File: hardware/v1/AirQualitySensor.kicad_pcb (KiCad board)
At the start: 2 copper layers, 81.3 x 36.8 mm, 44 parts, among them J1 USB_C_Receptacle_USB2.0, J2 SWD, J3 UART, U1 004-0-0053, U2 DHT22, U3 XC6206P332MR

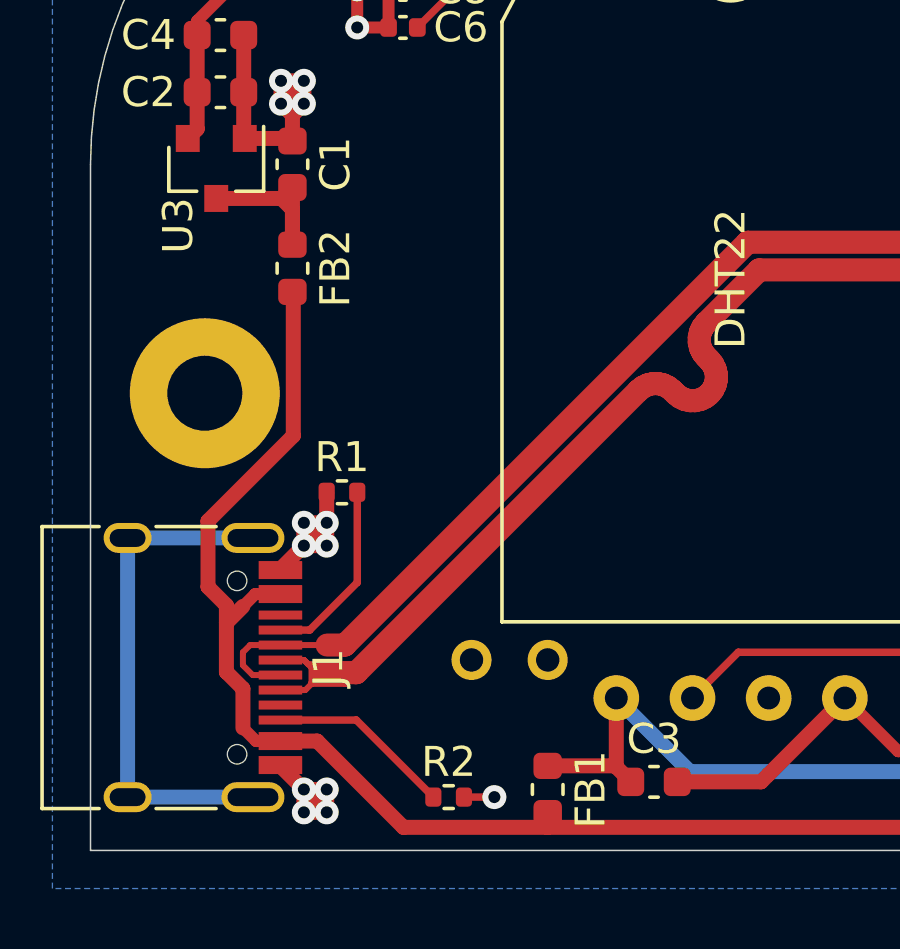
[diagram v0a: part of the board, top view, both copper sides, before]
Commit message: Fix ferrite bead having wrong footprint
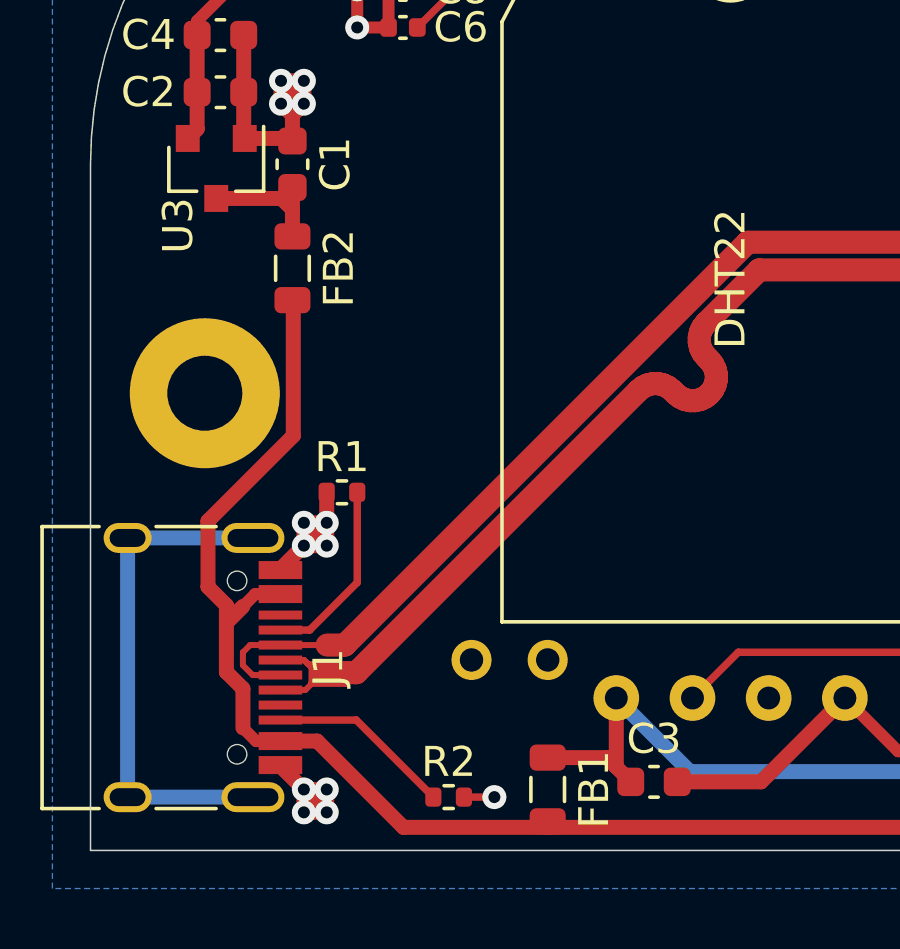
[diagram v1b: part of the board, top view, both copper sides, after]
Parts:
- C14, C5: value 100u -> 100n
- FB1, FB2: footprint Inductor_SMD:L_0603_1608Metric -> Inductor_SMD:L_0805_2012Metric
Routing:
- net Net-(C1-Pad2): track 6.29 -> 4.84 mm
- net VBUS: track 98.1 -> 97.6 mm

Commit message: Fix Status1 LED typo
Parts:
- D5: value Status0 -> Status1
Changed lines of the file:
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@@
       (drillshape 0)
       (scaleselection 1)
-      (outputdirectory "release/gerber/"))
+      (outputdirectory "release/gerber"))
   )
   (net 0 "")
@@
       (effects (font (size 1 1) (thickness 0.15)))
     )
-    (fp_text value Status0 (at 0 1.65 90) (layer F.Fab)
-      (effects (font (size 1 1) (thickness 0.15)))
-    )
+    (fp_text value Status1 (at 0 1.65 90) (layer F.Fab)
+      (effects (font (size 1 1) (thickness 0.15)))
+    )
